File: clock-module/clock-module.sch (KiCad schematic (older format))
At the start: 17 parts

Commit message: Add logic gates datasheets, add timer selection circuit schematics
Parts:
- removed C?: 0.01uF, symbol Device:C
- removed C?: 1uF, symbol Device:CP
- removed C? (x3): C, symbol Device:C
- removed R? (x2): 1k, symbol Device:R
- removed R? (x4): R, symbol Device:R
- removed RV?: 1M, symbol Device:R_POT_TRIM
- removed SW?: SW_Push, symbol Switch:SW_Push
- removed SW?: SW_SPDT, symbol Switch:SW_SPDT
- removed U? (x3): LM555, symbol Timer:LM555
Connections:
- net labels removed: GND, VCC, astable-clk-out-net, astable-clk-tr
- wire segments 18 -> 0
- no-connect marks 1 -> 0
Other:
- note added: "Astable LMC555 Timer"
- note added: "Connectors"
- note added: "Monostable LMC555 Timer"
- note added: "Timer Selection Circuit"
- note removed: "Astable LM555 Timer"

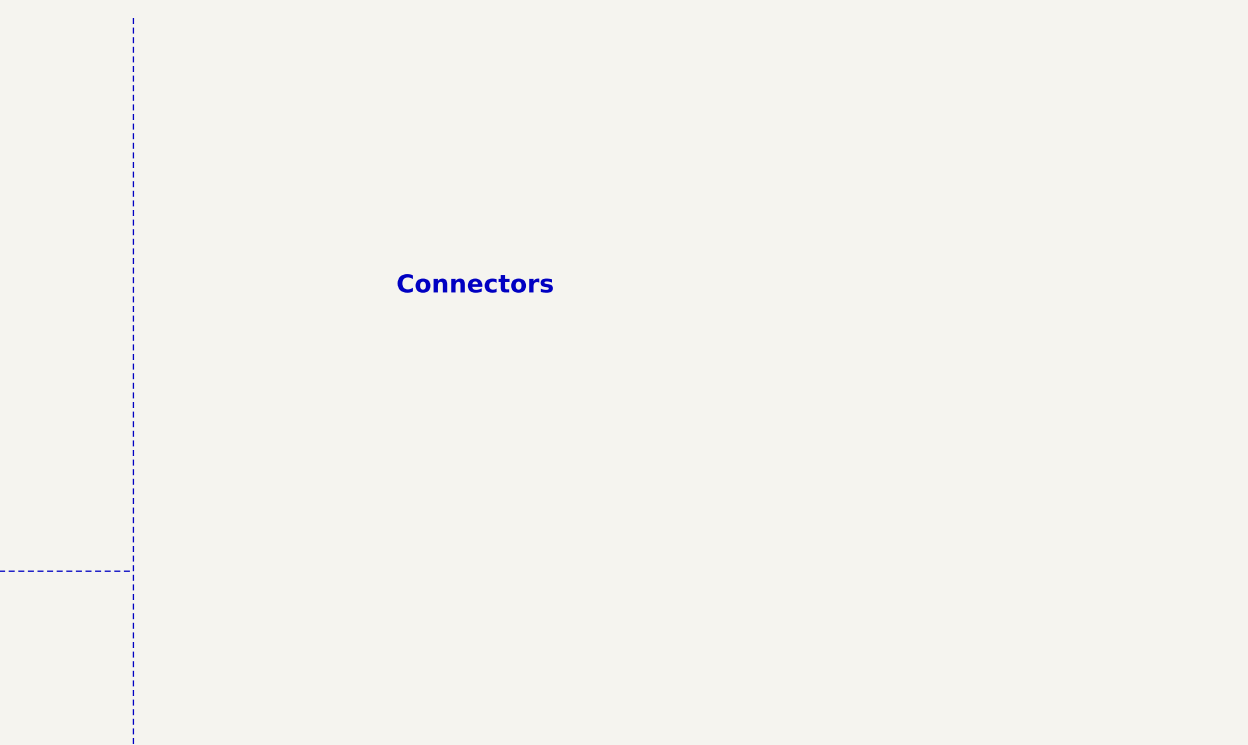
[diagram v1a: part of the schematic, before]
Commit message: Add connectors to clock module
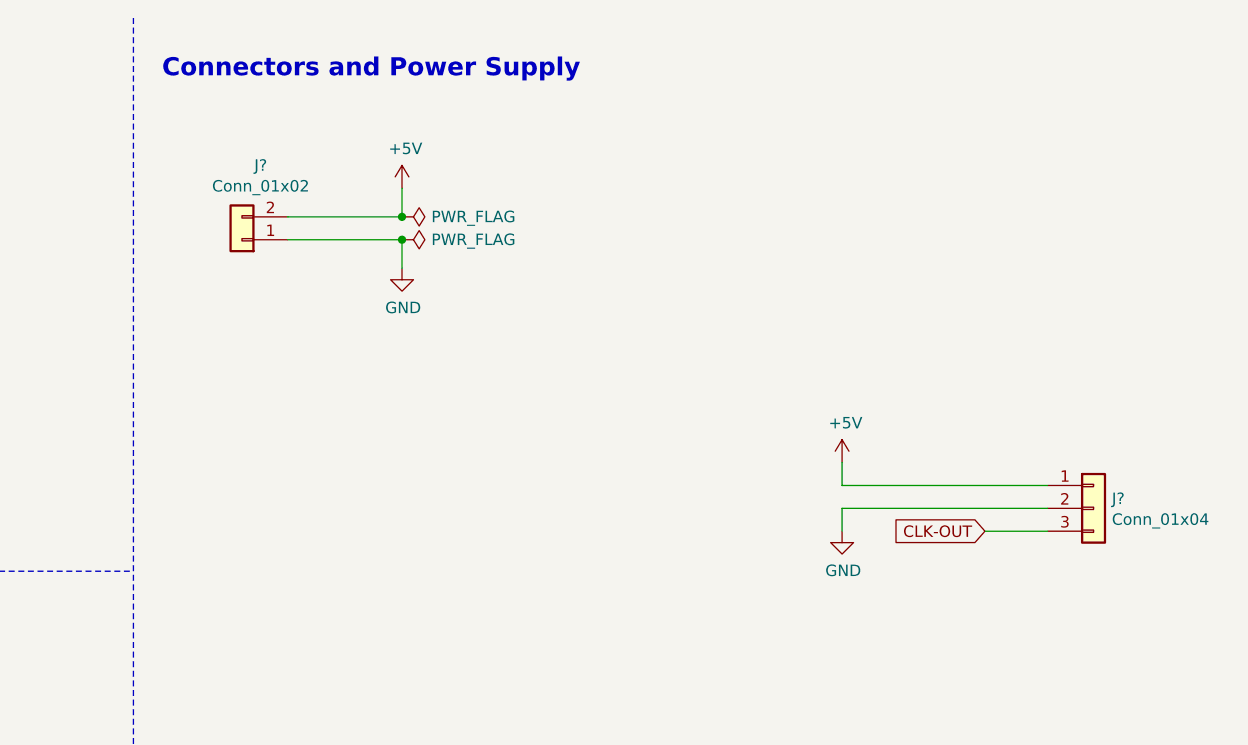
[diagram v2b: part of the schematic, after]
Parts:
- added J?: Conn_01x02, symbol Connector_Generic:Conn_01x02
- added J?: Conn_01x04, symbol Connector_Generic:Conn_01x03
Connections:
- new net +5V: J?.1 (Pin_1), J?.2 (Pin_2)
- new net CLK-OUT: J?.3 (Pin_3)
- new net GND: J?.1 (Pin_1), J?.2 (Pin_2)
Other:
- note added: "Connectors and Power Supply"
- note removed: "Connectors"
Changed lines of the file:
@@
 Sheet 1 4
 Title "Clock module"
-Date "2019-07-10"
+Date "2019-07-13"
 Rev "1"
 Comp ""
-Comment1 "\"8 bit computer\" project by Ben Eater"
-Comment2 "From breadboard to PCB by Damiano Lodi"
+Comment1 "Adapted from Damiano Lodi"
+Comment2 "\"8 bit computer\" project by Ben Eater"
 Comment3 ""
 Comment4 ""
@@
 Wire Notes Line
 	475  2900 5850 2900
-Text Notes 7000 1700 0    79   ~ 16
-Connectors
+Text Notes 5975 750  0    79   ~ 16
+Connectors and Power Supply
+$Comp
+L Connector_Generic:Conn_01x02 J?
+U 1 1 5D299965
+P 6325 1450
+F 0 "J?" H 6243 1125 50  0000 C CNN
+F 1 "Conn_01x02" H 6243 1216 50  0000 C CNN
+F 2 "" H 6325 1450 50  0001 C CNN
+F 3 "~" H 6325 1450 50  0001 C CNN
+	1    6325 1450
+	-1   0    0    1
+$EndComp
+$Comp
+L power:+5V #PWR?
+U 1 1 5D29A606
+P 7025 1225
+F 0 "#PWR?" H 7025 1075 50  0001 C CNN
+F 1 "+5V" H 7040 1398 50  0000 C CNN
+F 2 "" H 7025 1225 50  0001 C CNN
+F 3 "" H 7025 1225 50  0001 C CNN
+	1    7025 1225
+	1    0    0    -1
+$EndComp
+$Comp
+L power:GND #PWR?
+U 1 1 5D29B8C6
+P 7025 1575
+F 0 "#PWR?" H 7025 1325 50  0001 C CNN
+F 1 "GND" H 7030 1402 50  0000 C CNN
+F 2 "" H 7025 1575 50  0001 C CNN
+F 3 "" H 7025 1575 50  0001 C CNN
+	1    7025 1575
+	1    0    0    -1
+$EndComp
+Wire Wire Line
+	6525 1350 7025 1350
+Wire Wire Line
+	7025 1350 7025 1225
+Wire Wire Line
+	6525 1450 7025 1450
+Wire Wire Line
+	7025 1450 7025 1575
+$Comp
+L power:PWR_FLAG #FLG?
+U 1 1 5D29C6F5
+P 7025 1350
+F 0 "#FLG?" H 7025 1425 50  0001 C CNN
+F 1 "PWR_FLAG" V 7025 1478 50  0000 L CNN
+F 2 "" H 7025 1350 50  0001 C CNN
+F 3 "~" H 7025 1350 50  0001 C CNN
+	1    7025 1350
+	0    1    1    0
+$EndComp
+Connection ~ 7025 1350
+$Comp
+L power:PWR_FLAG #FLG?
+U 1 1 5D29CE65
+P 7025 1450
+F 0 "#FLG?" H 7025 1525 50  0001 C CNN
+F 1 "PWR_FLAG" V 7025 1578 50  0000 L CNN
+F 2 "" H 7025 1450 50  0001 C CNN
+F 3 "~" H 7025 1450 50  0001 C CNN
+	1    7025 1450
+	0    1    1    0
+$EndComp
+Connection ~ 7025 1450
+$Comp
+L Connector_Generic:Conn_01x03 J?
+U 1 1 5D29DA49
+P 10050 2625
+F 0 "J?" H 10130 2667 50  0000 L CNN
+F 1 "Conn_01x04" H 10130 2576 50  0000 L CNN
+F 2 "" H 10050 2625 50  0001 C CNN
+F 3 "~" H 10050 2625 50  0001 C CNN
+	1    10050 2625
+	1    0    0    -1
+$EndComp
+$Comp
+L power:GND #PWR?
+U 1 1 5D2A2021
+P 8950 2725
+F 0 "#PWR?" H 8950 2475 50  0001 C CNN
+F 1 "GND" H 8955 2552 50  0000 C CNN
+F 2 "" H 8950 2725 50  0001 C CNN
+F 3 "" H 8950 2725 50  0001 C CNN
+	1    8950 2725
+	1    0    0    -1
+$EndComp
+$Comp
+L power:+5V #PWR?
+U 1 1 5D2A294C
+P 8950 2425
+F 0 "#PWR?" H 8950 2275 50  0001 C CNN
+F 1 "+5V" H 8965 2598 50  0000 C CNN
+F 2 "" H 8950 2425 50  0001 C CNN
+F 3 "" H 8950 2425 50  0001 C CNN
+	1    8950 2425
+	1    0    0    -1
+$EndComp
+Text GLabel 9575 2725 0    50   Input ~ 0
+CLK-OUT
+Wire Wire Line
+	9575 2725 9850 2725
+Wire Wire Line
+	8950 2425 8950 2525
+Wire Wire Line
+	8950 2525 9850 2525
+Wire Wire Line
+	9850 2625 8950 2625
+Wire Wire Line
+	8950 2625 8950 2725
 $EndSCHEMATC

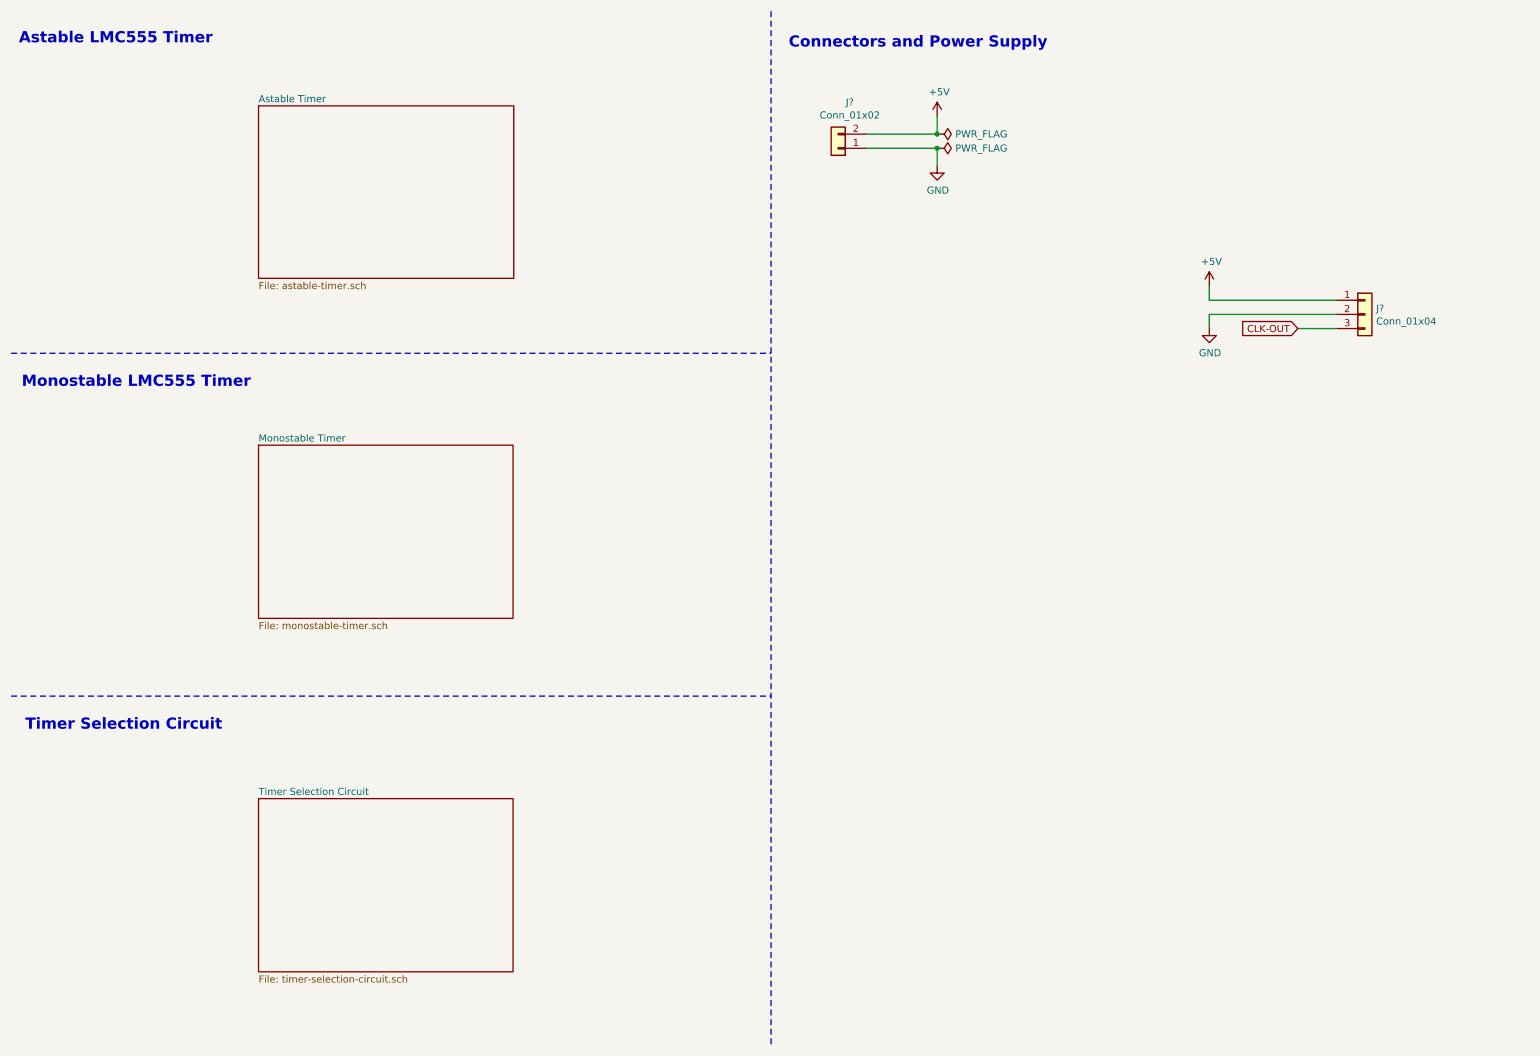
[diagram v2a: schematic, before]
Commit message: Add LED to all outputs of clocl-module
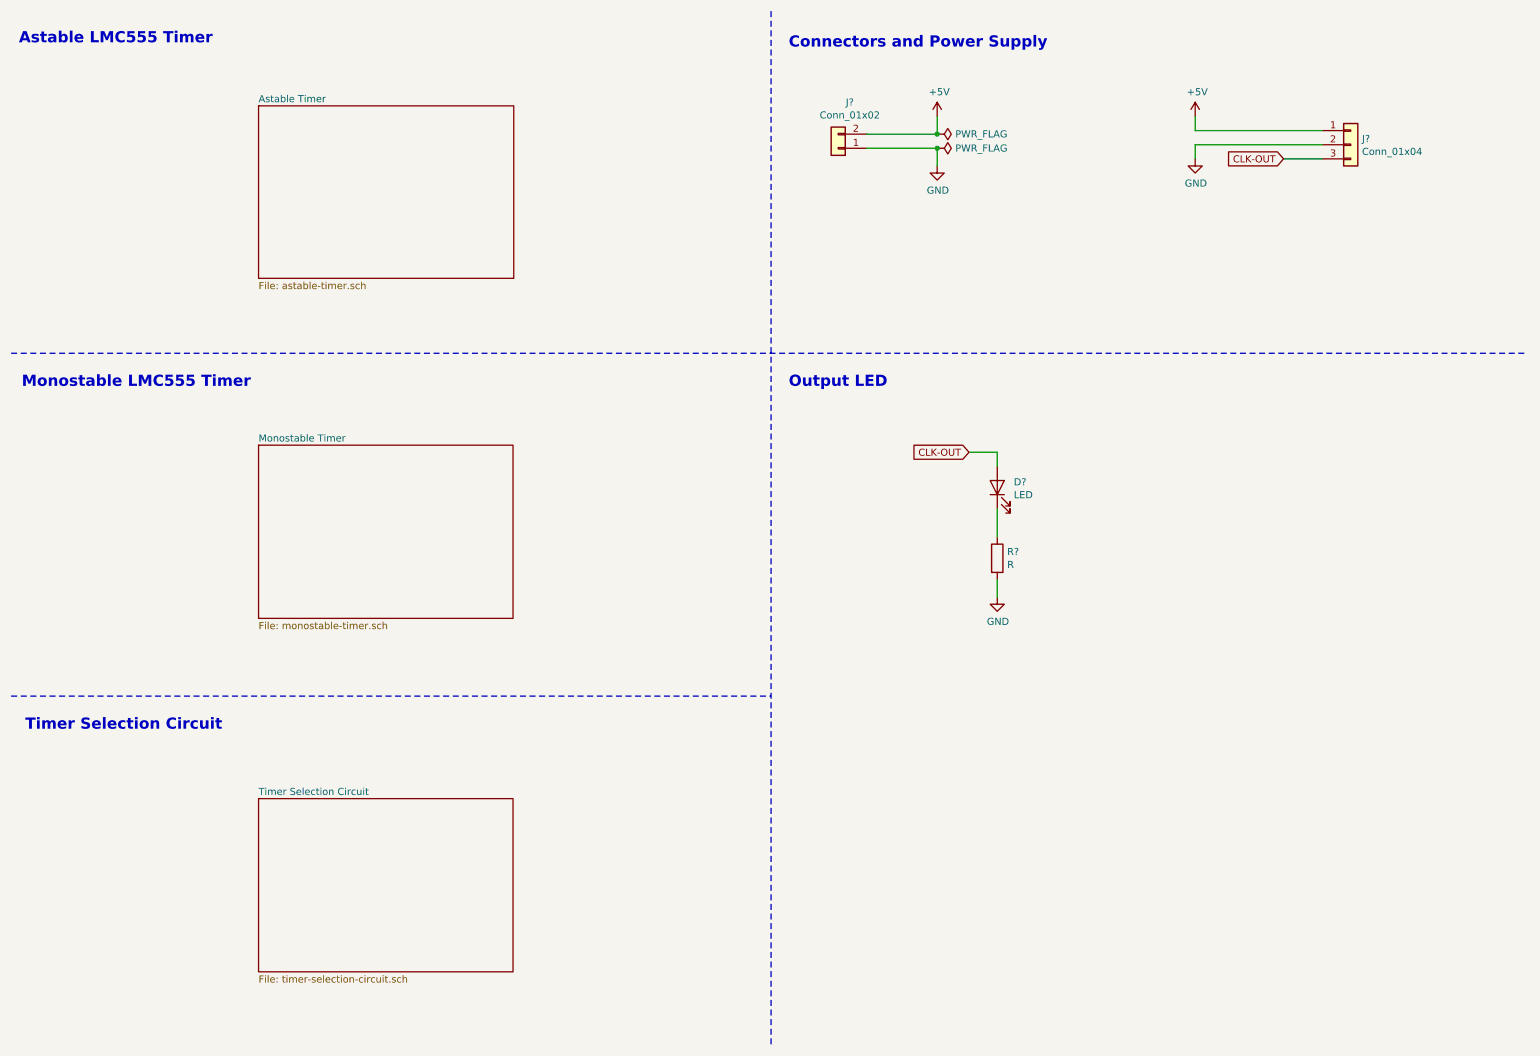
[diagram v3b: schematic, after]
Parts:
- added D?: LED, symbol Device:LED
- added R?: R, symbol Device:R
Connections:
- net CLK-OUT: now also D?.2 (A)
- net GND: now also R?.2
- new net: D?.1 (K), R?.1
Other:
- note added: "Output LED"
- moved on the sheet: J?
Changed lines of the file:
@@
 Text Notes 575  5575 0    79   ~ 16
 Timer Selection Circuit
-Wire Notes Line
-	475  2900 5850 2900
 Text Notes 5975 750  0    79   ~ 16
 Connectors and Power Supply
@@
 L Connector_Generic:Conn_01x03 J?
 U 1 1 5D29DA49
-P 10050 2625
-F 0 "J?" H 10130 2667 50  0000 L CNN
-F 1 "Conn_01x04" H 10130 2576 50  0000 L CNN
-F 2 "" H 10050 2625 50  0001 C CNN
-F 3 "~" H 10050 2625 50  0001 C CNN
-	1    10050 2625
+P 9950 1425
+F 0 "J?" H 10030 1467 50  0000 L CNN
+F 1 "Conn_01x04" H 10030 1376 50  0000 L CNN
+F 2 "" H 9950 1425 50  0001 C CNN
+F 3 "~" H 9950 1425 50  0001 C CNN
+	1    9950 1425
 	1    0    0    -1
 $EndComp
@@
 L power:GND #PWR?
 U 1 1 5D2A2021
-P 8950 2725
-F 0 "#PWR?" H 8950 2475 50  0001 C CNN
-F 1 "GND" H 8955 2552 50  0000 C CNN
-F 2 "" H 8950 2725 50  0001 C CNN
-F 3 "" H 8950 2725 50  0001 C CNN
-	1    8950 2725
+P 8850 1525
+F 0 "#PWR?" H 8850 1275 50  0001 C CNN
+F 1 "GND" H 8855 1352 50  0000 C CNN
+F 2 "" H 8850 1525 50  0001 C CNN
+F 3 "" H 8850 1525 50  0001 C CNN
+	1    8850 1525
 	1    0    0    -1
 $EndComp
@@
 L power:+5V #PWR?
 U 1 1 5D2A294C
-P 8950 2425
-F 0 "#PWR?" H 8950 2275 50  0001 C CNN
-F 1 "+5V" H 8965 2598 50  0000 C CNN
-F 2 "" H 8950 2425 50  0001 C CNN
-F 3 "" H 8950 2425 50  0001 C CNN
-	1    8950 2425
+P 8850 1225
+F 0 "#PWR?" H 8850 1075 50  0001 C CNN
+F 1 "+5V" H 8865 1398 50  0000 C CNN
+F 2 "" H 8850 1225 50  0001 C CNN
+F 3 "" H 8850 1225 50  0001 C CNN
+	1    8850 1225
 	1    0    0    -1
 $EndComp
-Text GLabel 9575 2725 0    50   Input ~ 0
+Text GLabel 9475 1525 0    50   Input ~ 0
 CLK-OUT
 Wire Wire Line
-	9575 2725 9850 2725
+	9475 1525 9750 1525
 Wire Wire Line
-	8950 2425 8950 2525
+	8850 1225 8850 1325
 Wire Wire Line
-	8950 2525 9850 2525
+	8850 1325 9750 1325
 Wire Wire Line
-	9850 2625 8950 2625
+	9750 1425 8850 1425
 Wire Wire Line
-	8950 2625 8950 2725
+	8850 1425 8850 1525
+Wire Notes Line
+	475  2900 11200 2900
+Text Notes 5975 3150 0    79   ~ 16
+Output LED
+Text GLabel 7250 3600 0    50   Input ~ 0
+CLK-OUT
+$Comp
+L Device:R R?
+U 1 1 5D2B7458
+P 7450 4350
+F 0 "R?" H 7520 4396 50  0000 L CNN
+F 1 "R" H 7520 4305 50  0000 L CNN
+F 2 "" V 7380 4350 50  0001 C CNN
+F 3 "~" H 7450 4350 50  0001 C CNN
+	1    7450 4350
+	1    0    0    -1
+$EndComp
+$Comp
+L Device:LED D?
+U 1 1 5D2B783D
+P 7450 3850
+F 0 "D?" V 7489 3733 50  0000 R CNN
+F 1 "LED" V 7398 3733 50  0000 R CNN
+F 2 "" H 7450 3850 50  0001 C CNN
+F 3 "~" H 7450 3850 50  0001 C CNN
+	1    7450 3850
+	0    -1   -1   0
+$EndComp
+$Comp
+L power:GND #PWR?
+U 1 1 5D2B972F
+P 7450 4625
+F 0 "#PWR?" H 7450 4375 50  0001 C CNN
+F 1 "GND" H 7455 4452 50  0000 C CNN
+F 2 "" H 7450 4625 50  0001 C CNN
+F 3 "" H 7450 4625 50  0001 C CNN
+	1    7450 4625
+	1    0    0    -1
+$EndComp
+Wire Wire Line
+	7250 3600 7450 3600
+Wire Wire Line
+	7450 3600 7450 3700
+Wire Wire Line
+	7450 4000 7450 4200
+Wire Wire Line
+	7450 4500 7450 4625
 $EndSCHEMATC

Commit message: Add clock inverter to clock-module, correct label directions
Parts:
- added Q?: Q_NMOS_DGS, symbol Device:Q_NMOS_DGS
- added Q?: Q_PMOS_DGS, symbol Device:Q_PMOS_DGS
- J?: symbol Connector_Generic:Conn_01x03 -> Connector_Generic:Conn_01x04
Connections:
- net +5V: now also Q?.1 (D)
- net CLK-OUT: now also Q?.2 (G), Q?.2 (G)
- net GND: now also Q?.3 (S)
- new net ~CLK-OUT: J?.4 (Pin_4), Q?.1 (D), Q?.3 (S)
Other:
- note added: "Clock Inverter"
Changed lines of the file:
@@
 Connection ~ 7025 1450
 $Comp
-L Connector_Generic:Conn_01x03 J?
+L Connector_Generic:Conn_01x04 J?
 U 1 1 5D29DA49
 P 9950 1425
@@
 Wire Wire Line
 	7450 4500 7450 4625
+Wire Notes Line
+	8525 2900 8525 6525
+Text Notes 8650 3175 0    79   ~ 16
+Clock Inverter
+Text GLabel 9025 4575 0    50   Input ~ 0
+CLK-OUT
+$Comp
+L Device:Q_NMOS_DGS Q?
+U 1 1 5D2BBA8E
+P 9500 4850
+F 0 "Q?" H 9706 4896 50  0000 L CNN
+F 1 "Q_NMOS_DGS" H 9706 4805 50  0000 L CNN
+F 2 "" H 9700 4950 50  0001 C CNN
+F 3 "~" H 9500 4850 50  0001 C CNN
+	1    9500 4850
+	1    0    0    -1
+$EndComp
+$Comp
+L Device:Q_PMOS_DGS Q?
+U 1 1 5D2BC068
+P 9500 4325
+F 0 "Q?" H 9706 4371 50  0000 L CNN
+F 1 "Q_PMOS_DGS" H 9706 4280 50  0000 L CNN
+F 2 "" H 9700 4425 50  0001 C CNN
+F 3 "~" H 9500 4325 50  0001 C CNN
+	1    9500 4325
+	1    0    0    -1
+$EndComp
+$Comp
+L power:GND #PWR?
+U 1 1 5D2BD4A8
+P 9600 5300
+F 0 "#PWR?" H 9600 5050 50  0001 C CNN
+F 1 "GND" H 9605 5127 50  0000 C CNN
+F 2 "" H 9600 5300 50  0001 C CNN
+F 3 "" H 9600 5300 50  0001 C CNN
+	1    9600 5300
+	1    0    0    -1
+$EndComp
+$Comp
+L power:+5V #PWR?
+U 1 1 5D2BD8BB
+P 9600 3975
+F 0 "#PWR?" H 9600 3825 50  0001 C CNN
+F 1 "+5V" H 9615 4148 50  0000 C CNN
+F 2 "" H 9600 3975 50  0001 C CNN
+F 3 "" H 9600 3975 50  0001 C CNN
+	1    9600 3975
+	1    0    0    -1
+$EndComp
+Wire Wire Line
+	9025 4575 9200 4575
+Wire Wire Line
+	9200 4575 9200 4325
+Wire Wire Line
+	9200 4325 9300 4325
+Wire Wire Line
+	9300 4850 9200 4850
+Wire Wire Line
+	9200 4850 9200 4575
+Connection ~ 9200 4575
+Wire Wire Line
+	9600 4125 9600 3975
+Wire Wire Line
+	9600 4525 9600 4575
+Wire Wire Line
+	9600 5300 9600 5050
+Wire Wire Line
+	9600 4575 10025 4575
+Connection ~ 9600 4575
+Wire Wire Line
+	9600 4575 9600 4650
+Text GLabel 10025 4575 2    50   Output ~ 0
+~CLK-OUT
+Text GLabel 9475 1675 0    50   Input ~ 0
+~CLK-OUT
+Wire Wire Line
+	9475 1675 9625 1675
+Wire Wire Line
+	9625 1675 9625 1625
+Wire Wire Line
+	9625 1625 9750 1625
 $EndSCHEMATC
